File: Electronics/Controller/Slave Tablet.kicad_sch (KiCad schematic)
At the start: 11 parts, among them J16 SLAVE TABLET, U14 FT232RL, U15 FT232RL

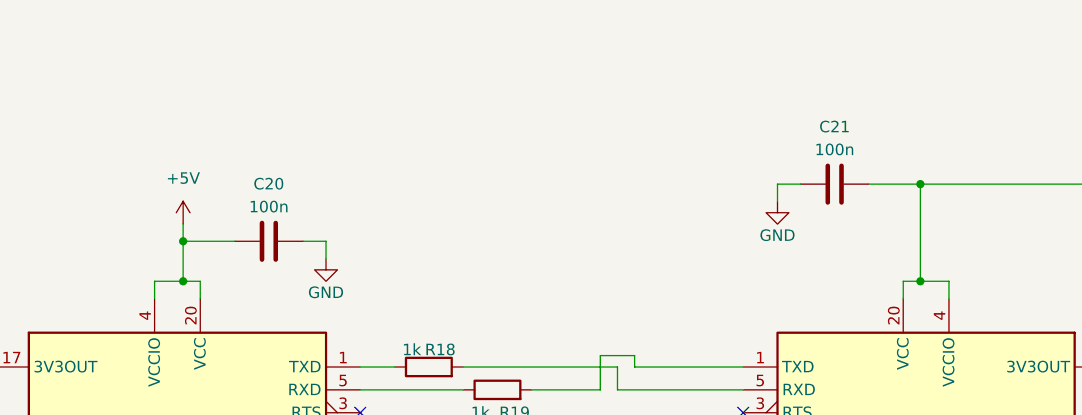
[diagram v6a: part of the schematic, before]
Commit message: Added 4.7uF caps to FT232RL on controller.
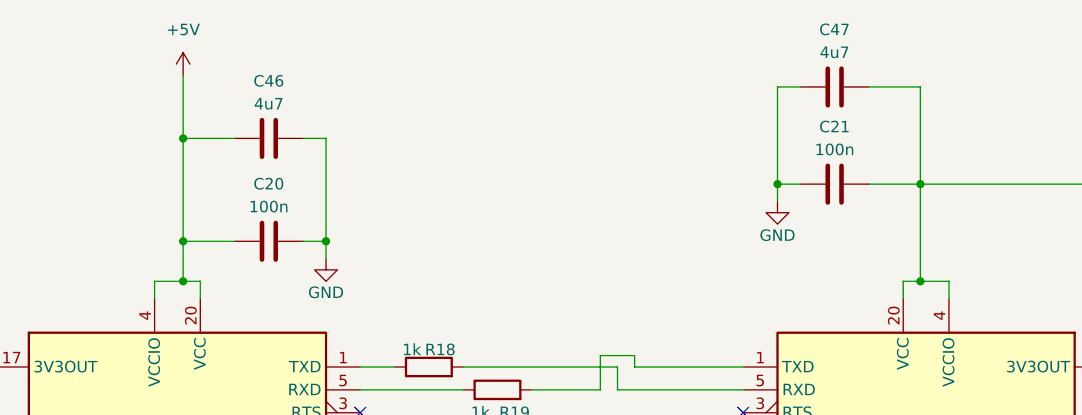
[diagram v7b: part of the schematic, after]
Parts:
- added C46, C47: 4u7, Capacitor_SMD:C_0805_2012Metric, symbol Device:C
- C19, C20, C21, C22: LCSC (none) -> C1711
- C23: LCSC (none) -> C1710
- J16: LCSC (none) -> C428495
- R18, R19: LCSC (none) -> C17513
- U14, U15: LCSC (none) -> C8690
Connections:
- net +5V: now also C46.1
- net GND: now also C46.2, C47.1
- net at C21.1, C23.1, FB1.1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: now also C47.2
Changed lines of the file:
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@@
   (title_block
     (title "Tandem Leveller Controller")
-    (date "2025-02-22")
+    (date "2025-03-11")
     (rev "V1.0")
     (company "(C) andy@britishideas.com 2025")
@@
   (junction (at 176.53 127) (diameter 0) (color 0 0 0 0)
   )
+  (junction (at 112.395 67.945) (diameter 0) (color 0 0 0 0)
+  )
   (junction (at 184.15 127) (diameter 0) (color 0 0 0 0)
   )
@@
   (junction (at 179.07 127) (diameter 0) (color 0 0 0 0)
   )
+  (junction (at 96.52 56.515) (diameter 0) (color 0 0 0 0)
+  )
   (junction (at 211.455 61.595) (diameter 0) (color 0 0 0 0)
   )
@@
   )
   (junction (at 238.76 101.6) (diameter 0) (color 0 0 0 0)
+  )
+  (junction (at 162.56 61.595) (diameter 0) (color 0 0 0 0)
   )
   (no_connect (at 158.75 112.395))
@@
     (stroke (width 0) (type default))
   )
+  (wire (pts (xy 165.1 50.8) (xy 162.56 50.8))
+    (stroke (width 0) (type default))
+  )
   (wire (pts (xy 200.66 81.915) (xy 199.39 81.915))
     (stroke (width 0) (type default))
@@
     (stroke (width 0) (type default))
   )
+  (wire (pts (xy 178.435 50.8) (xy 178.435 61.595))
+    (stroke (width 0) (type default))
+  )
   (wire (pts (xy 144.78 84.455) (xy 158.75 84.455))
     (stroke (width 0) (type default))
@@
     (stroke (width 0) (type default))
   )
+  (wire (pts (xy 112.395 56.515) (xy 112.395 67.945))
+    (stroke (width 0) (type default))
+  )
   (wire (pts (xy 95.885 125.095) (xy 95.885 127))
     (stroke (width 0) (type default))
@@
     (stroke (width 0) (type default))
   )
-  (wire (pts (xy 96.52 66.04) (xy 96.52 67.945))
+  (wire (pts (xy 96.52 49.53) (xy 96.52 56.515))
+    (stroke (width 0) (type default))
+  )
+  (wire (pts (xy 162.56 50.8) (xy 162.56 61.595))
     (stroke (width 0) (type default))
   )
@@
     (stroke (width 0) (type default))
   )
+  (wire (pts (xy 172.72 50.8) (xy 178.435 50.8))
+    (stroke (width 0) (type default))
+  )
   (wire (pts (xy 236.22 99.695) (xy 236.22 101.6))
     (stroke (width 0) (type default))
@@
     (stroke (width 0) (type default))
   )
+  (wire (pts (xy 109.855 56.515) (xy 112.395 56.515))
+    (stroke (width 0) (type default))
+  )
   (wire (pts (xy 211.455 64.135) (xy 211.455 61.595))
     (stroke (width 0) (type default))
@@
     (stroke (width 0) (type default))
   )
+  (wire (pts (xy 96.52 56.515) (xy 102.235 56.515))
+    (stroke (width 0) (type default))
+  )
   (wire (pts (xy 199.39 92.075) (xy 228.6 92.075))
     (stroke (width 0) (type default))
@@
   )
   (wire (pts (xy 90.805 127) (xy 95.885 127))
+    (stroke (width 0) (type default))
+  )
+  (wire (pts (xy 96.52 56.515) (xy 96.52 67.945))
     (stroke (width 0) (type default))
   )
@@
     (effects (font (size 1.27 1.27)) (justify right))
   )
-  (symbol (lib_id "power:+5V") (at 96.52 66.04 0) (unit 1)
+  (symbol (lib_id "power:+5V") (at 96.52 49.53 0) (unit 1)
     (in_bom yes) (on_board yes) (dnp no) (fields_autoplaced)
-    (property "Reference" "#PWR050" (at 96.52 69.85 0)
-      (effects (font (size 1.27 1.27)) hide)
-    )
-    (property "Value" "+5V" (at 96.52 60.96 0)
-      (effects (font (size 1.27 1.27)))
-    )
-    (property "Footprint" "" (at 96.52 66.04 0)
-      (effects (font (size 1.27 1.27)) hide)
-    )
-    (property "Datasheet" "" (at 96.52 66.04 0)
+    (property "Reference" "#PWR050" (at 96.52 53.34 0)
+      (effects (font (size 1.27 1.27)) hide)
+    )
+    (property "Value" "+5V" (at 96.52 44.45 0)
+      (effects (font (size 1.27 1.27)))
+    )
+    (property "Footprint" "" (at 96.52 49.53 0)
+      (effects (font (size 1.27 1.27)) hide)
+    )
+    (property "Datasheet" "" (at 96.52 49.53 0)
       (effects (font (size 1.27 1.27)) hide)
     )
@@
       (effects (font (size 1.27 1.27)) hide)
     )
+    (property "LCSC" "C1710" (at 211.455 67.945 0)
+      (effects (font (size 1.27 1.27)) hide)
+    )
     (pin "1")
     (pin "2")
@@
     )
   )
+  (symbol (lib_id "Device:C") (at 168.91 50.8 90) (unit 1)
+    (in_bom yes) (on_board yes) (dnp no)
+    (property "Reference" "C47" (at 168.91 44.45 90)
+      (effects (font (size 1.27 1.27)))
+    )
+    (property "Value" "4u7" (at 168.91 46.99 90)
+      (effects (font (size 1.27 1.27)))
+    )
+    (property "Footprint" "Capacitor_SMD:C_0805_2012Metric" (at 172.72 49.8348 0)
+      (effects (font (size 1.27 1.27)) hide)
+    )
+    (property "Datasheet" "~" (at 168.91 50.8 0)
+      (effects (font (size 1.27 1.27)) hide)
+    )
+    (property "LCSC" "" (at 168.91 50.8 0)
+      (effects (font (size 1.27 1.27)) hide)
+    )
+    (pin "1")
+    (pin "2")
+    (instances
+      (project "Tandem Leveller Controller"
+        (path "/56ffd1a6-bbed-43b6-8aa8-f23f49f76448/996de356-8852-43bb-9787-2c246f9a1860"
+          (reference "C47") (unit 1)
+        )
+      )
+    )
+  )
   (symbol (lib_id "power:GND") (at 176.53 128.905 0) (mirror y) (unit 1)
     (in_bom yes) (on_board yes) (dnp no) (fields_autoplaced)
@@
       (effects (font (size 1.27 1.27)) hide)
     )
+    (property "LCSC" "C1711" (at 67.945 81.915 0)
+      (effects (font (size 1.27 1.27)) hide)
+    )
     (pin "1")
     (pin "2")
@@
     )
     (property "Datasheet" "https://www.ftdichip.com/Support/Documents/DataSheets/ICs/DS_FT232R.pdf" (at 179.07 99.695 0)
+      (effects (font (size 1.27 1.27)) hide)
+    )
+    (property "LCSC" "C8690" (at 179.07 99.695 0)
       (effects (font (size 1.27 1.27)) hide)
     )
@@
       (effects (font (size 1.27 1.27)) hide)
     )
+    (property "LCSC" "C1711" (at 204.47 81.915 0)
+      (effects (font (size 1.27 1.27)) hide)
+    )
     (pin "1")
     (pin "2")
@@
       (effects (font (size 1.27 1.27)) hide)
     )
+    (property "LCSC" "" (at 222.885 67.945 0)
+      (effects (font (size 1.27 1.27)) hide)
+    )
     (pin "1")
     (pin "2")
@@
       (effects (font (size 1.27 1.27)) hide)
     )
+    (property "LCSC" "C17513" (at 123.825 81.915 0)
+      (effects (font (size 1.27 1.27)) hide)
+    )
     (pin "1")
     (pin "2")
@@
       (effects (font (size 1.27 1.27)) hide)
     )
+    (property "LCSC" "C1711" (at 168.91 61.595 0)
+      (effects (font (size 1.27 1.27)) hide)
+    )
     (pin "1")
     (pin "2")
@@
     )
   )
+  (symbol (lib_id "Device:C") (at 106.045 56.515 90) (unit 1)
+    (in_bom yes) (on_board yes) (dnp no)
+    (property "Reference" "C46" (at 106.045 50.165 90)
+      (effects (font (size 1.27 1.27)))
+    )
+    (property "Value" "4u7" (at 106.045 52.705 90)
+      (effects (font (size 1.27 1.27)))
+    )
+    (property "Footprint" "Capacitor_SMD:C_0805_2012Metric" (at 109.855 55.5498 0)
+      (effects (font (size 1.27 1.27)) hide)
+    )
+    (property "Datasheet" "~" (at 106.045 56.515 0)
+      (effects (font (size 1.27 1.27)) hide)
+    )
+    (property "LCSC" "" (at 106.045 56.515 0)
+      (effects (font (size 1.27 1.27)) hide)
+    )
+    (pin "1")
+    (pin "2")
+    (instances
+      (project "Tandem Leveller Controller"
+        (path "/56ffd1a6-bbed-43b6-8aa8-f23f49f76448/996de356-8852-43bb-9787-2c246f9a1860"
+          (reference "C46") (unit 1)
+        )
+      )
+    )
+  )
   (symbol (lib_id "Connector:USB_B_Mini") (at 236.22 89.535 0) (mirror y) (unit 1)
     (in_bom yes) (on_board yes) (dnp no)
@@
     )
     (property "manf#" "10103594-0001LF" (at 236.22 89.535 0)
+      (effects (font (size 1.27 1.27)) hide)
+    )
+    (property "LCSC" "C428495" (at 236.22 89.535 0)
       (effects (font (size 1.27 1.27)) hide)
     )
@@
     )
     (property "Datasheet" "https://www.ftdichip.com/Support/Documents/DataSheets/ICs/DS_FT232R.pdf" (at 95.885 99.695 0)
+      (effects (font (size 1.27 1.27)) hide)
+    )
+    (property "LCSC" "C8690" (at 95.885 99.695 0)
       (effects (font (size 1.27 1.27)) hide)
     )
@@
       (effects (font (size 1.27 1.27)) hide)
     )
+    (property "LCSC" "C17513" (at 131.445 84.455 0)
+      (effects (font (size 1.27 1.27)) hide)
+    )
     (pin "1")
     (pin "2")
@@
       (effects (font (size 1.27 1.27)) hide)
     )
+    (property "LCSC" "C1711" (at 106.045 67.945 0)
+      (effects (font (size 1.27 1.27)) hide)
+    )

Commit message: Removed JLCPCB part numbers for Teensy and BNO085 connectors. Added JLCPCB part number for 4.7uF capacitor. Generated JLCPCB manufacturing files for all boards.
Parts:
- C46, C47: LCSC (none) -> C1779
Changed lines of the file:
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@@
       (effects (font (size 1.27 1.27)) hide)
     )
-    (property "LCSC" "" (at 168.91 50.8 0)
+    (property "LCSC" "C1779" (at 168.91 50.8 0)
       (effects (font (size 1.27 1.27)) hide)
     )
@@
       (effects (font (size 1.27 1.27)) hide)
     )
-    (property "LCSC" "" (at 106.045 56.515 0)
-      (effects (font (size 1.27 1.27)) hide)
-    )
+    (property "LCSC" "C1779" (at 106.045 56.515 0)
+      (effects (font (size 1.27 1.27)) hide)
+    )
